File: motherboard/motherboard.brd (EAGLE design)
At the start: 105.1 x 137.2 mm, 51 parts, among them IC1 USB6B1, Q1 MOSFET-NCHANNELPTH2, T1 2N3904, T2 2N3904, U1 LED_100V_BUCK, U2 LED_100V_BUCK, U3 LED_100V_BUCK, U4 LED_100V_BUCK, X1 USB_3P-85-32003-00X-1

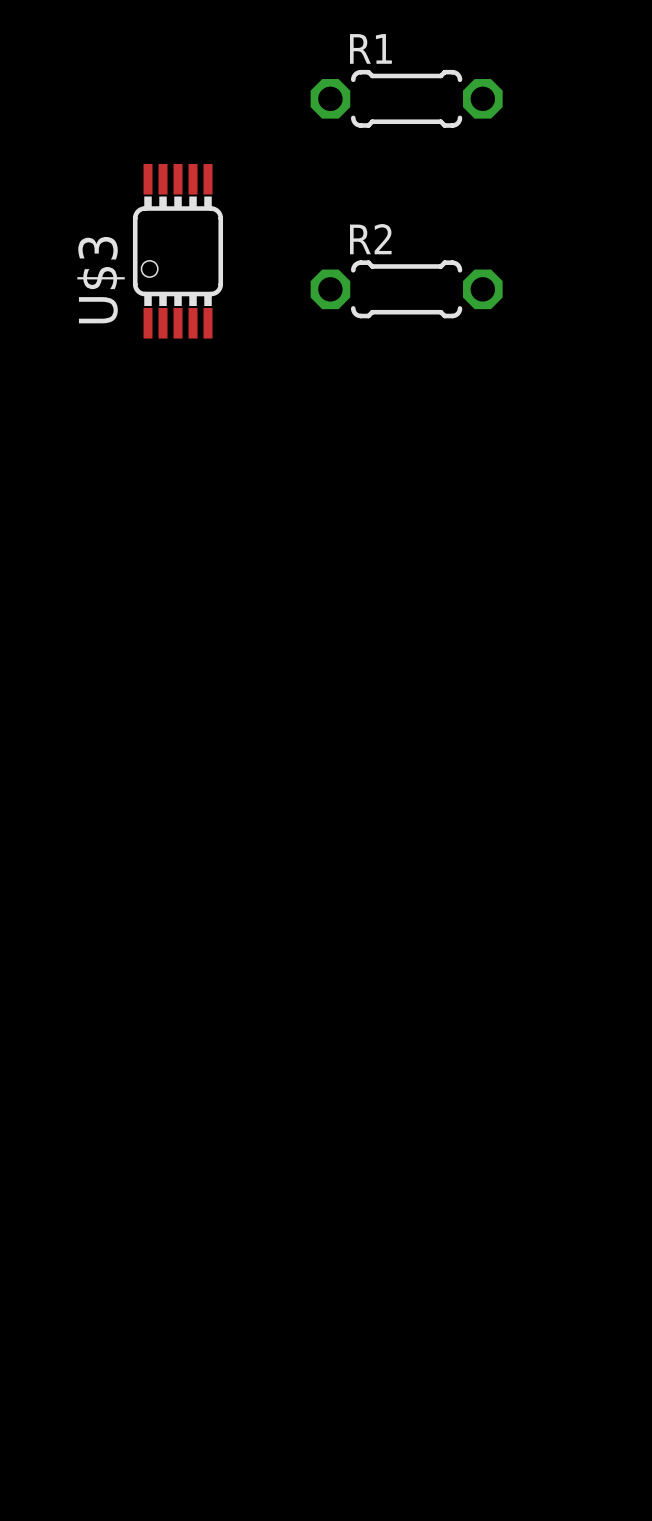
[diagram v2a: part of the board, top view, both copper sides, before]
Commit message: Finish adding voltage monitoring IC.
Generate bill of materials.
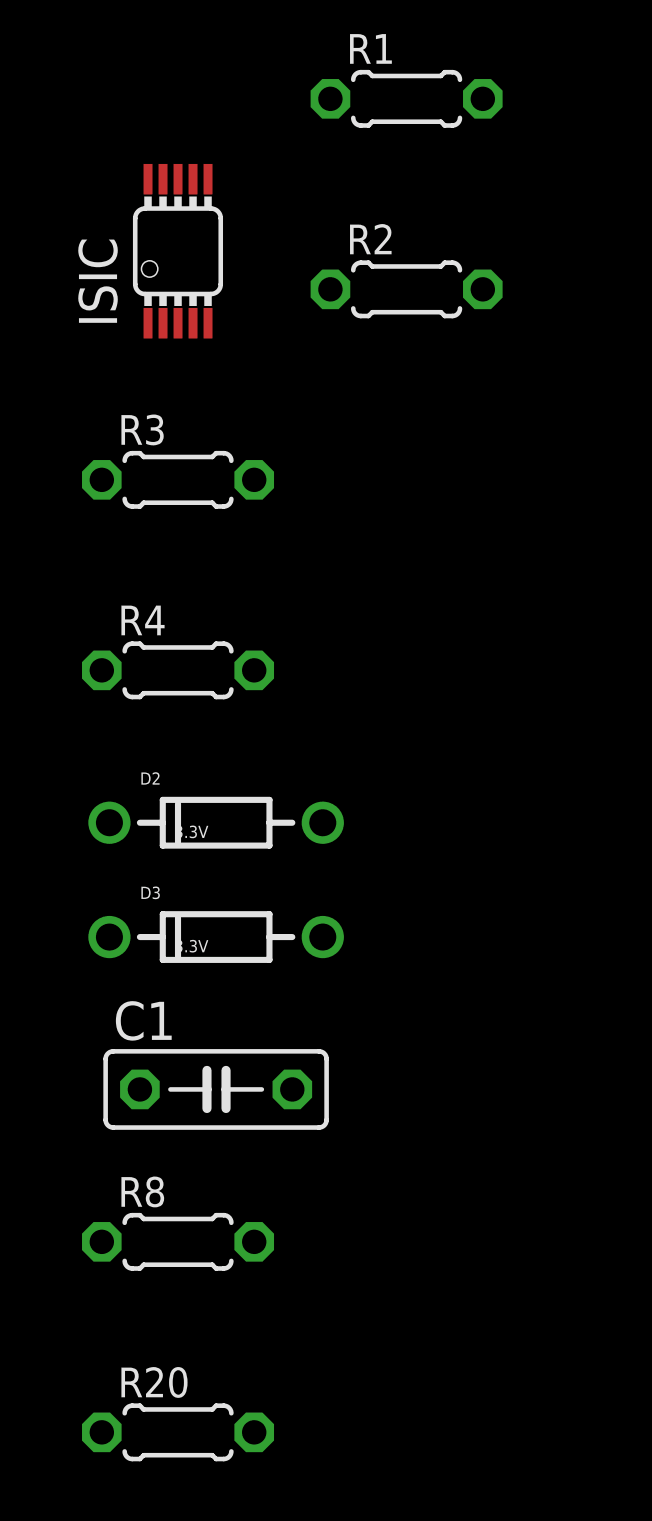
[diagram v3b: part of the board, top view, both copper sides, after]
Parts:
- added C1: 0.1uF, rcl:C050-025X075
- added D2, D3: 3.3V, SparkFun-DiscreteSemi:DIODE-ZENER
- added R20, R8: 10k, rcl:0204/5
- added R3, R4: 33k, rcl:0204/5
- R1, R18: value 1M -> 965k
- R11, R6, R7: value 5k -> 965k
- R12: value 5k -> 33k
- renumbered U$3 to ISIC
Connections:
- new net N$21: ISIC.1, R20.1, R8.2
- net +3V3: now also C1.1, ISIC.10
- net +5V: now also R8.1
- net BATT_SENSE: now also ISIC.2
- net GND: now also C1.2, D2.P$2, D3.P$2, ISIC.5, ISIC.8, ISIC.9, R20.2, R3.2, R4.2
- net N$12: now also D3.P$1, ISIC.3, R4.1
- net N$17: now also D2.P$1, ISIC.4, R3.1
- net SCL: now also ISIC.7
- net SDA: now also ISIC.6
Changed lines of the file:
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@@
 </element>
 <element name="OA1" library="SparkFun-AnalogIC" package="DIP08" value="LM358" x="22.86" y="21.59"/>
-<element name="R6" library="rcl" package="0204/5" value="5k" x="-46.99" y="118.11"/>
-<element name="R7" library="rcl" package="0204/5" value="5k" x="-54.61" y="118.11"/>
+<element name="R6" library="rcl" package="0204/5" value="965k" x="-46.99" y="118.11"/>
+<element name="R7" library="rcl" package="0204/5" value="965k" x="-54.61" y="118.11"/>
 <element name="MISSILE" library="SparkFun-Electromechanical" package="SWITCH-SPDT" value="" x="-97.79" y="63.5"/>
 <element name="R9" library="SparkFun-Electromechanical" package="3362U-2" value="100k" x="-38.1" y="110.49"/>
 <element name="R10" library="rcl" package="0204/5" value="50K" x="-62.23" y="118.11"/>
-<element name="R11" library="rcl" package="0204/5" value="5k" x="-69.85" y="118.11"/>
-<element name="R12" library="rcl" package="0204/5" value="5k" x="-77.47" y="118.11"/>
+<element name="R11" library="rcl" package="0204/5" value="965k" x="-69.85" y="118.11"/>
+<element name="R12" library="rcl" package="0204/5" value="33k" x="-77.47" y="118.11"/>
 <element name="D1" library="SparkFun-DiscreteSemi" package="DIODE-ZENER" value="3.3V" x="-67.31" y="121.92"/>
 <element name="GRIP" library="con-amp-quick" package="05P" value="" x="101.6" y="44.45" rot="R90">
@@
 <element name="SPEED" library="SparkFun-Connectors" package="JST-2-PTH-KIT" value="" x="99.06" y="3.81" rot="R270"/>
 <element name="CADENCE" library="SparkFun-Connectors" package="JST-2-PTH-KIT" value="" x="99.06" y="10.16" rot="R270"/>
-<element name="R18" library="rcl" package="0204/5" value="1M" x="-111.76" y="-29.21"/>
+<element name="R18" library="rcl" package="0204/5" value="965k" x="-111.76" y="-29.21"/>
 <element name="R19" library="rcl" package="0204/5" value="36k" x="-111.76" y="-35.56"/>
-<element name="R1" library="rcl" package="0204/5" value="1M" x="-111.76" y="-41.91"/>
+<element name="R1" library="rcl" package="0204/5" value="965k" x="-111.76" y="-41.91"/>
 <element name="R2" library="rcl" package="0204/5" value="25k" x="-111.76" y="-48.26"/>
-<element name="U$3" library="droidcycle" package="MSOP10" value="LTC2990" x="-119.38" y="-46.99"/>
+<element name="ISIC" library="droidcycle" package="MSOP10" value="LTC2990" x="-119.38" y="-46.99"/>
+<element name="R3" library="rcl" package="0204/5" value="33k" x="-119.38" y="-54.61"/>
+<element name="R4" library="rcl" package="0204/5" value="33k" x="-119.38" y="-60.96"/>
+<element name="D2" library="SparkFun-DiscreteSemi" package="DIODE-ZENER" value="3.3V" x="-118.11" y="-66.04"/>
+<element name="D3" library="SparkFun-DiscreteSemi" package="DIODE-ZENER" value="3.3V" x="-118.11" y="-69.85"/>
+<element name="C1" library="rcl" package="C050-025X075" value="0.1uF" x="-118.11" y="-74.93"/>
+<element name="R8" library="rcl" package="0204/5" value="10k" x="-119.38" y="-80.01"/>
+<element name="R20" library="rcl" package="0204/5" value="10k" x="-119.38" y="-86.36"/>
 </elements>
 <signals>
@@
 <contactref element="R2" pad="1"/>
 <contactref element="IC1" pad="4"/>
-<wire x1="-114.3" y1="-35.56" x2="-114.3" y2="-48.26" width="0" layer="19" extent="1-1"/>
+<contactref element="R3" pad="2"/>
+<contactref element="R4" pad="2"/>
+<contactref element="D2" pad="P$2"/>
+<contactref element="D3" pad="P$2"/>
+<contactref element="ISIC" pad="5"/>
+<contactref element="C1" pad="2"/>
+<contactref element="ISIC" pad="9"/>
+<contactref element="ISIC" pad="8"/>
+<contactref element="R20" pad="2"/>
+<wire x1="-115.57" y1="-74.93" x2="-116.84" y2="-86.36" width="0" layer="19" extent="1-1"/>
+<wire x1="-114.554" y1="-69.85" x2="-115.57" y2="-74.93" width="0" layer="19" extent="1-1"/>
+<wire x1="-114.554" y1="-66.04" x2="-114.554" y2="-69.85" width="0" layer="19" extent="1-1"/>
+<wire x1="-116.84" y1="-60.96" x2="-114.554" y2="-66.04" width="0" layer="19" extent="1-1"/>
+<wire x1="-116.84" y1="-54.61" x2="-116.84" y2="-60.96" width="0" layer="19" extent="1-1"/>
+<wire x1="-118.38" y1="-49.39" x2="-116.84" y2="-54.61" width="0" layer="19" extent="1-1"/>
+<wire x1="-114.3" y1="-48.26" x2="-118.38" y2="-49.39" width="0" layer="19" extent="1-1"/>
+<wire x1="-119.38" y1="-44.59" x2="-118.38" y2="-49.39" width="0" layer="19" extent="1-1"/>
+<wire x1="-119.88" y1="-44.59" x2="-119.38" y2="-44.59" width="0" layer="19" extent="1-1"/>
+<wire x1="-114.3" y1="-35.56" x2="-119.38" y2="-44.59" width="0" layer="19" extent="1-1"/>
 <wire x1="-87.63" y1="9.445625" x2="-114.3" y2="-35.56" width="0" layer="19" extent="1-1"/>
 <wire x1="-63.5" y1="9.445625" x2="-87.63" y2="9.445625" width="0" layer="19" extent="1-1"/>
@@
 <contactref element="R14" pad="1"/>
 <contactref element="R13" pad="1"/>
-<wire x1="101.6" y1="39.37" x2="97.87" y2="53.88" width="0" layer="19" extent="1-1"/>
-<wire x1="101.6" y1="20.32" x2="101.6" y2="39.37" width="0" layer="19" extent="1-1"/>
-<wire x1="52.07" y1="2.54" x2="101.6" y2="20.32" width="0" layer="19" extent="1-1"/>
-<wire x1="6.27" y1="47.45" x2="52.07" y2="2.54" width="0" layer="19" extent="1-1"/>
+<contactref element="ISIC" pad="10"/>
+<contactref element="C1" pad="1"/>
+<wire x1="-120.38" y1="-44.59" x2="-120.65" y2="-74.93" width="0" layer="19" extent="1-1"/>
+<wire x1="6.27" y1="47.45" x2="-120.38" y2="-44.59" width="0" layer="19" extent="1-1"/>
 <wire x1="7.54" y1="57.88" x2="6.27" y2="47.45" width="0" layer="19" extent="1-1"/>
 <wire x1="-39.9288" y1="98.0694" x2="7.54" y2="57.88" width="0" layer="19" extent="1-1"/>
@@
 <wire x1="-102.87" y1="118.11" x2="-95.25" y2="118.11" width="0" layer="19" extent="1-1"/>
 <wire x1="-110.49" y1="118.11" x2="-102.87" y2="118.11" width="0" layer="19" extent="1-1"/>
+<wire x1="52.07" y1="2.54" x2="6.27" y2="47.45" width="0" layer="19" extent="1-1"/>
+<wire x1="101.6" y1="20.32" x2="52.07" y2="2.54" width="0" layer="19" extent="1-1"/>
+<wire x1="101.6" y1="39.37" x2="101.6" y2="20.32" width="0" layer="19" extent="1-1"/>
+<wire x1="97.87" y1="53.88" x2="101.6" y2="39.37" width="0" layer="19" extent="1-1"/>
 </signal>
 <signal name="+5V">
@@
 <contactref element="PTC2" pad="1"/>
 <contactref element="IC1" pad="1"/>
+<contactref element="R8" pad="1"/>
+<wire x1="-114.3" y1="-17.78" x2="-121.92" y2="-80.01" width="0" layer="19" extent="1-1"/>
 <wire x1="6.35" y1="34.29" x2="-114.3" y2="-17.78" width="0" layer="19" extent="1-1"/>
 <wire x1="5.08" y1="72.39" x2="6.35" y2="34.29" width="0" layer="19" extent="1-1"/>
@@
 <signal name="N$17">
 <contactref element="R7" pad="1"/>
+<contactref element="ISIC" pad="4"/>
+<contactref element="R3" pad="1"/>
+<contactref element="D2" pad="P$1"/>
+<wire x1="-121.92" y1="-54.61" x2="-121.666" y2="-66.04" width="0" layer="19" extent="1-1"/>
+<wire x1="-118.88" y1="-49.39" x2="-121.92" y2="-54.61" width="0" layer="19" extent="1-1"/>
+<wire x1="-57.15" y1="118.11" x2="-118.88" y2="-49.39" width="0" layer="19" extent="1-1"/>
 </signal>
 <signal name="N$19">
@@
 <contactref element="R11" pad="2"/>
 <contactref element="R12" pad="1"/>
+<contactref element="ISIC" pad="2"/>
+<wire x1="-80.01" y1="118.11" x2="-119.88" y2="-49.39" width="0" layer="19" extent="1-1"/>
+<wire x1="-70.866" y1="121.92" x2="-80.01" y2="118.11" width="0" layer="19" extent="1-1"/>
 <wire x1="-67.31" y1="118.11" x2="-70.866" y2="121.92" width="0" layer="19" extent="1-1"/>
-<wire x1="-80.01" y1="118.11" x2="-70.866" y2="121.92" width="0" layer="19" extent="1-1"/>
 </signal>
 <signal name="GRIP_THROTTLE">
@@
 <contactref element="IR" pad="1"/>
 <contactref element="R16" pad="2"/>
-<wire x1="52.07" y1="35.56" x2="101.6" y2="15.24" width="0" layer="19" extent="1-1"/>
-<wire x1="-105.41" y1="118.11" x2="52.07" y2="35.56" width="0" layer="19" extent="1-1"/>
+<contactref element="ISIC" pad="7"/>
+<wire x1="-105.41" y1="118.11" x2="-118.88" y2="-44.59" width="0" layer="19" extent="1-1"/>
+<wire x1="52.07" y1="35.56" x2="-105.41" y2="118.11" width="0" layer="19" extent="1-1"/>
+<wire x1="101.6" y1="15.24" x2="52.07" y2="35.56" width="0" layer="19" extent="1-1"/>
 </signal>
 <signal name="SDA">
@@
 <contactref element="U$1" pad="28"/>
 <contactref element="R15" pad="2"/>
-<wire x1="52.07" y1="33.02" x2="101.6" y2="17.78" width="0" layer="19" extent="1-1"/>
-<wire x1="-97.79" y1="118.11" x2="52.07" y2="33.02" width="0" layer="19" extent="1-1"/>
+<contactref element="ISIC" pad="6"/>
+<wire x1="-97.79" y1="118.11" x2="-118.38" y2="-44.59" width="0" layer="19" extent="1-1"/>
+<wire x1="52.07" y1="33.02" x2="-97.79" y2="118.11" width="0" layer="19" extent="1-1"/>
+<wire x1="101.6" y1="17.78" x2="52.07" y2="33.02" width="0" layer="19" extent="1-1"/>
 </signal>
 <signal name="VU">
@@
 <signal name="N$12">
 <contactref element="R6" pad="1"/>
+<contactref element="ISIC" pad="3"/>
+<contactref element="R4" pad="1"/>
+<contactref element="D3" pad="P$1"/>
+<wire x1="-121.92" y1="-60.96" x2="-121.666" y2="-69.85" width="0" layer="19" extent="1-1"/>
+<wire x1="-119.38" y1="-49.39" x2="-121.92" y2="-60.96" width="0" layer="19" extent="1-1"/>
+<wire x1="-49.53" y1="118.11" x2="-119.38" y2="-49.39" width="0" layer="19" extent="1-1"/>
 </signal>
 <signal name="PHOTO1">
@@
 <wire x1="88.63" y1="12.87" x2="88.265" y2="22.8" width="0" layer="19" extent="1-1"/>
 </signal>
+<signal name="N$21">
+<contactref element="R20" pad="1"/>
+<contactref element="R8" pad="2"/>
+<contactref element="ISIC" pad="1"/>
+<wire x1="-116.84" y1="-80.01" x2="-121.92" y2="-86.36" width="0" layer="19" extent="1-1"/>
+<wire x1="-120.38" y1="-49.39" x2="-116.84" y2="-80.01" width="0" layer="19" extent="1-1"/>
+</signal>
 </signals>

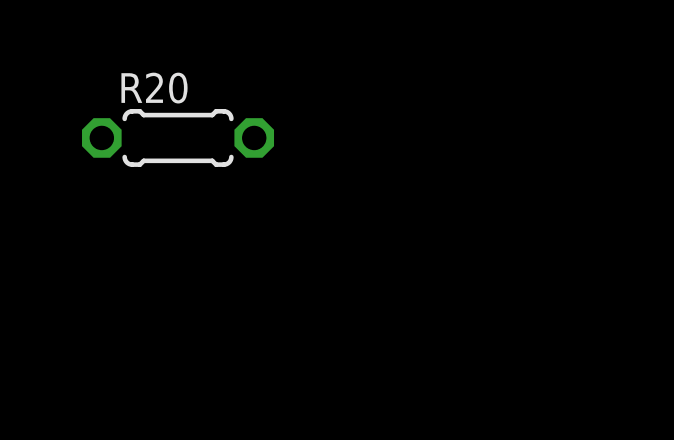
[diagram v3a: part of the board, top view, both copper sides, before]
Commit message: Add driver for missile switch led and reexport files.
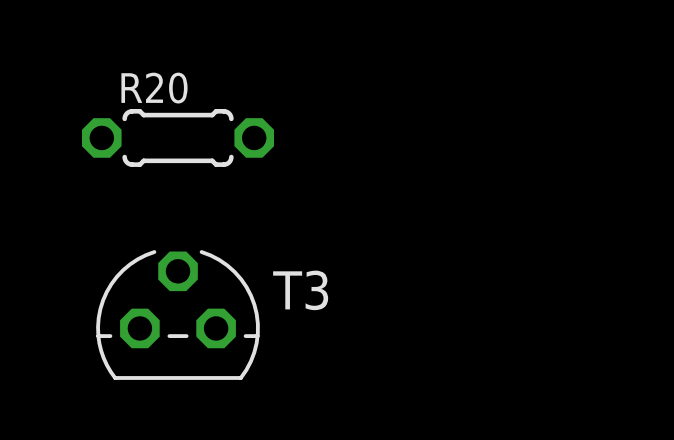
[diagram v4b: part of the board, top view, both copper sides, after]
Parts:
- added T3: 2N3904, transistor:TO92
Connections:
- new net MISSILE_LED: T3.1
- new net N$22: T3.2, U$1.10
- net GND: now also T3.3
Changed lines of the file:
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@@
 <element name="R8" library="rcl" package="0204/5" value="10k" x="-119.38" y="-80.01"/>
 <element name="R20" library="rcl" package="0204/5" value="10k" x="-119.38" y="-86.36"/>
+<element name="T3" library="transistor" package="TO92" value="2N3904" x="-119.38" y="-92.71"/>
 </elements>
 <signals>
@@
 <contactref element="ISIC" pad="8"/>
 <contactref element="R20" pad="2"/>
+<contactref element="T3" pad="3"/>
+<wire x1="-116.84" y1="-86.36" x2="-120.65" y2="-92.71" width="0" layer="19" extent="1-1"/>
 <wire x1="-115.57" y1="-74.93" x2="-116.84" y2="-86.36" width="0" layer="19" extent="1-1"/>
 <wire x1="-114.554" y1="-69.85" x2="-115.57" y2="-74.93" width="0" layer="19" extent="1-1"/>
@@
 <wire x1="-120.38" y1="-49.39" x2="-116.84" y2="-80.01" width="0" layer="19" extent="1-1"/>
 </signal>
+<signal name="MISSILE_LED">
+<contactref element="T3" pad="1"/>
+</signal>
+<signal name="N$22">
+<contactref element="U$1" pad="10"/>
+<contactref element="T3" pad="2"/>
+<wire x1="74.93" y1="25.4" x2="-119.38" y2="-90.805" width="0" layer="19" extent="1-1"/>
+</signal>
 </signals>

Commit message: Fix wiring of LED fault signal and leble LED indicator signal.
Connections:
- net N$22 renamed INDICATOR
- net /LED_FAULT: now also U$1.9
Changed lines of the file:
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@@
 <contactref element="U2" pad="JL4"/>
 <contactref element="U1" pad="JL4"/>
-<wire x1="-49.53" y1="50.085625" x2="-41.91" y2="118.11" width="0" layer="19" extent="1-1"/>
+<contactref element="U$1" pad="9"/>
+<wire x1="-25.4" y1="50.085625" x2="74.93" y2="22.86" width="0" layer="19" extent="1-1"/>
+<wire x1="-49.53" y1="50.085625" x2="-25.4" y2="50.085625" width="0" layer="19" extent="1-1"/>
 <wire x1="-73.66" y1="50.085625" x2="-49.53" y2="50.085625" width="0" layer="19" extent="1-1"/>
 <wire x1="-97.79" y1="50.085625" x2="-73.66" y2="50.085625" width="0" layer="19" extent="1-1"/>
-<wire x1="-25.4" y1="50.085625" x2="-49.53" y2="50.085625" width="0" layer="19" extent="1-1"/>
+<wire x1="-41.91" y1="118.11" x2="-49.53" y2="50.085625" width="0" layer="19" extent="1-1"/>
 </signal>
 <signal name="PWM0">
@@
 <contactref element="T3" pad="1"/>
 </signal>
-<signal name="N$22">
+<signal name="INDICATOR">
 <contactref element="U$1" pad="10"/>
 <contactref element="T3" pad="2"/>
